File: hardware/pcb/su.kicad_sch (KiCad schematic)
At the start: 22 parts, among them Q2 BC817

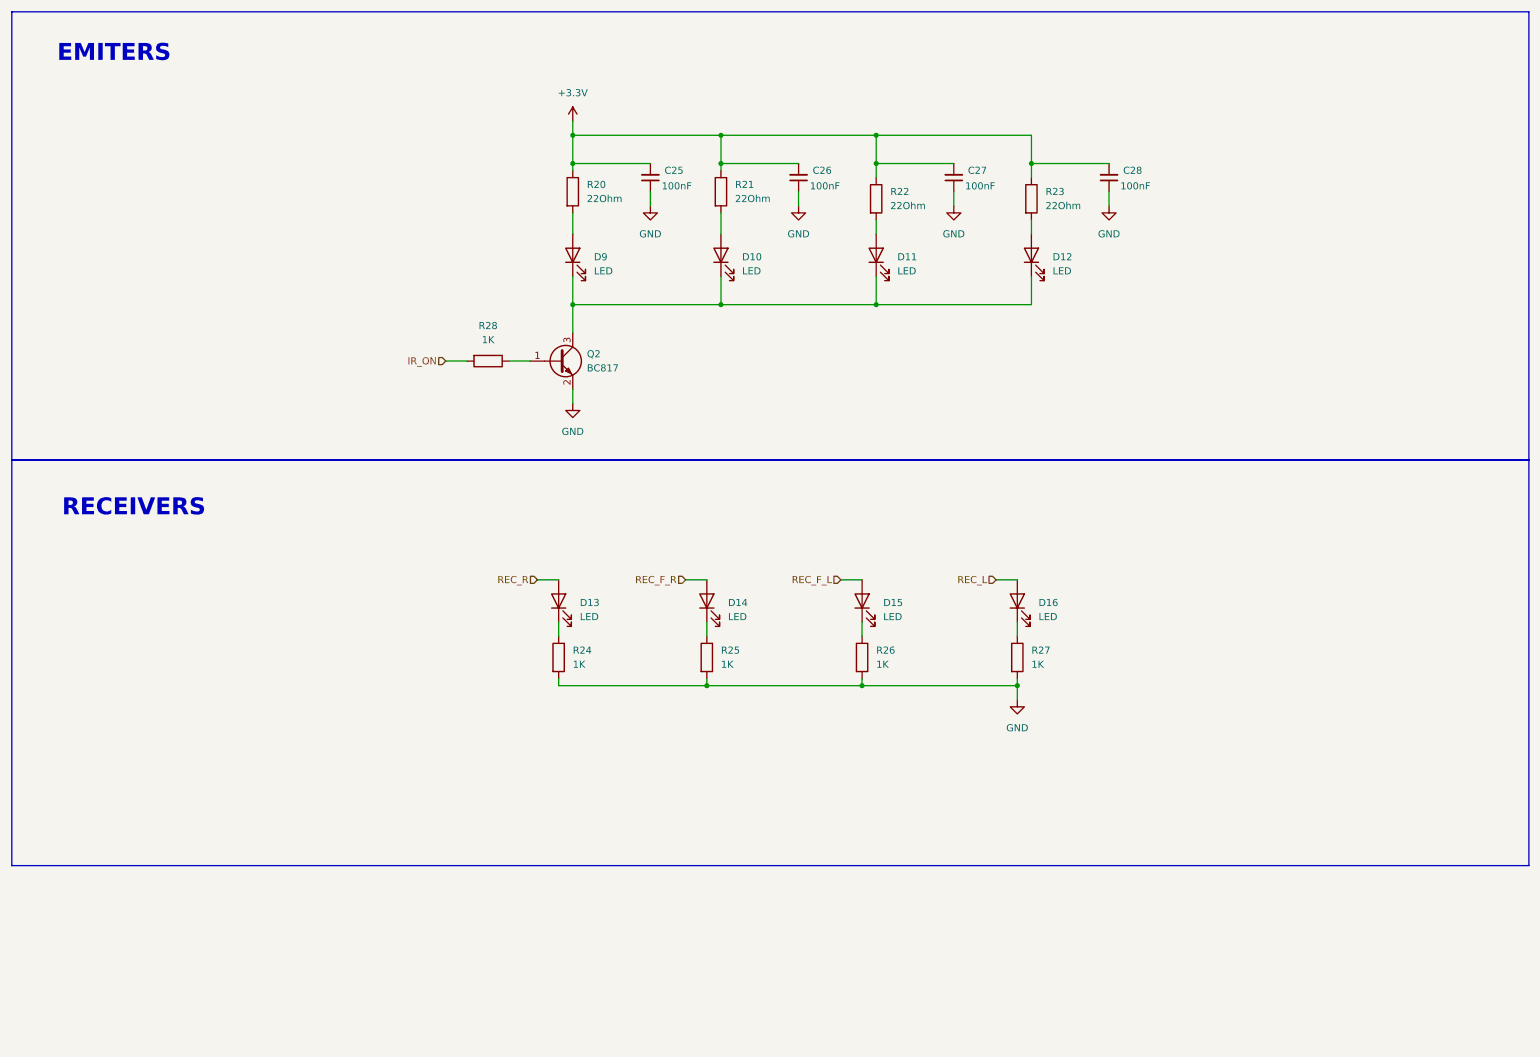
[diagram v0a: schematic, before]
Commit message: hardware: freeze schematic v1 after complete PCB redesign
Complete PCB and schematic refresh with reorganized sheets (psu, ui),
updated MCU/motor/sensor subsystems, and v1 schematic baseline frozen.
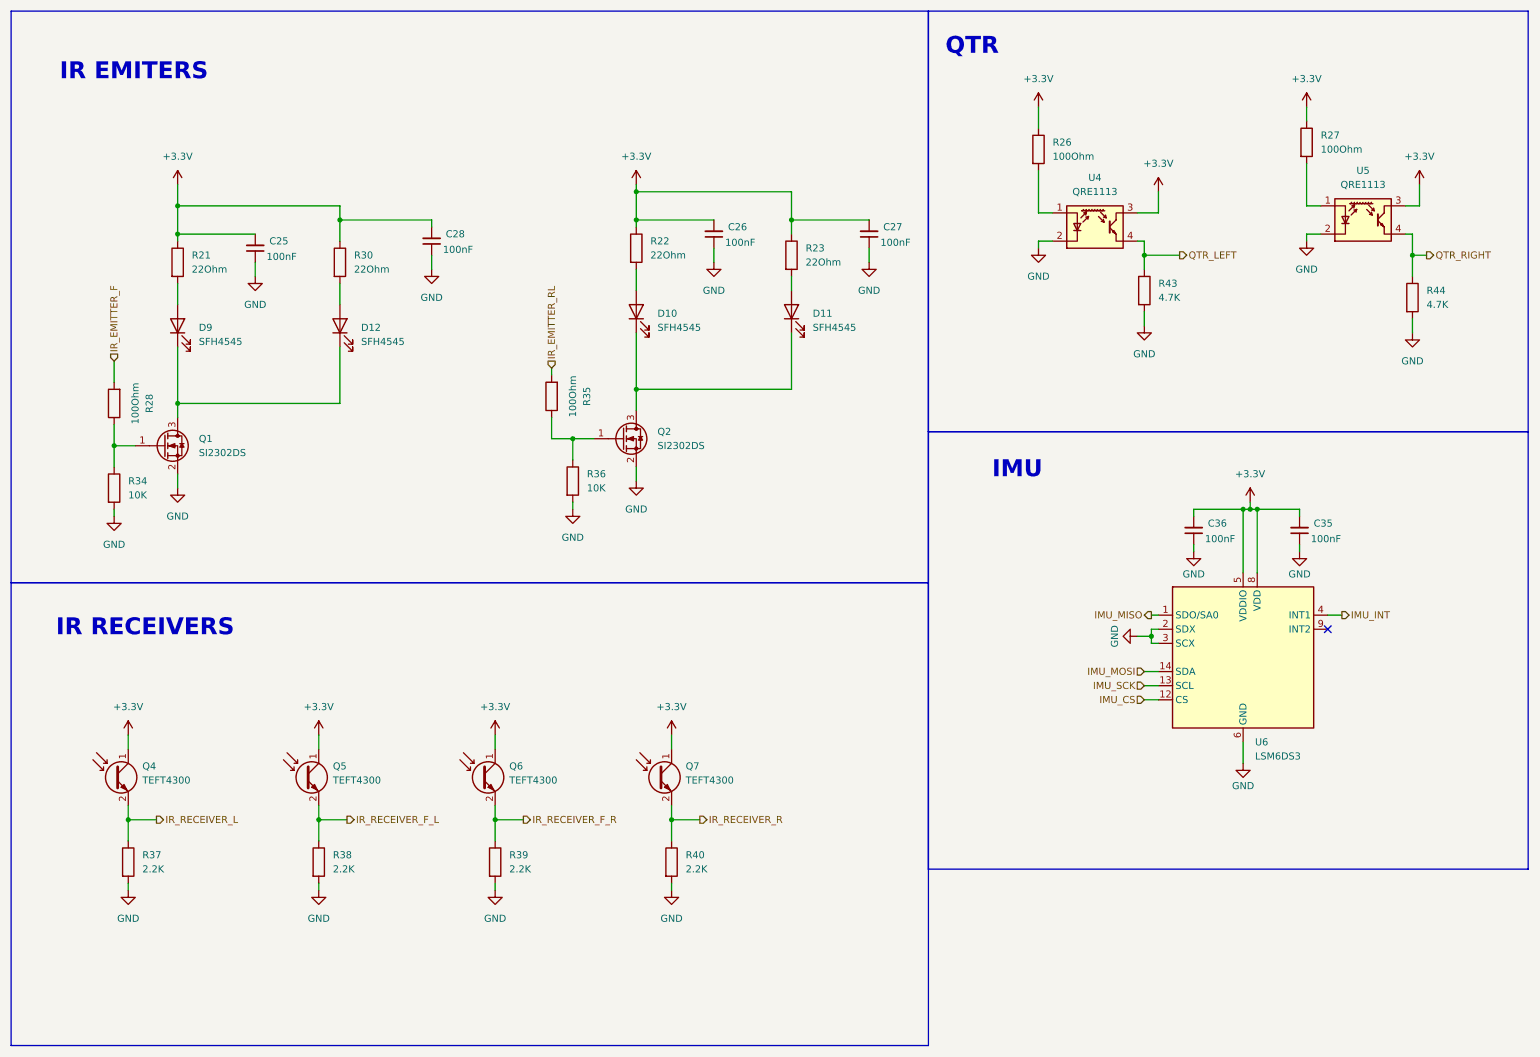
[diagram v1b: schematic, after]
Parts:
- removed D13, D14, D15, D16: LED, LED_THT:LED_D5.0mm, symbol Device:LED
- removed Q2: BC817, Package_TO_SOT_SMD:SOT-23, symbol Transistor_BJT:BC817
- removed R20: 22Ohm, Resistor_SMD:R_0805_2012Metric_Pad1.20x1.40mm_HandSolder, symbol Device:R
- removed R24, R25: 1K, Resistor_SMD:R_0805_2012Metric_Pad1.20x1.40mm_HandSolder, symbol Device:R
- added C35, C36: 100nF, Capacitor_SMD:C_0805_2012Metric_Pad1.18x1.45mm_HandSolder, symbol Device:C_Small
- added Q1, Q2: SI2302DS, Package_TO_SOT_SMD:SOT-23, symbol Transistor_FET:Q_NMOS_GSD
- added Q4, Q5, Q6, Q7: TEFT4300, LED_THT:LED_D3.0mm_IRBlack, symbol Device:Q_Photo_NPN
- added R30: 22Ohm, Resistor_SMD:R_1206_3216Metric_Pad1.30x1.75mm_HandSolder, symbol Device:R
- added R34, R36: 10K, Resistor_SMD:R_0805_2012Metric_Pad1.20x1.40mm_HandSolder, symbol Device:R
- added R35: 100Ohm, Resistor_SMD:R_0805_2012Metric_Pad1.20x1.40mm_HandSolder, symbol Device:R
- added R37, R38, R39, R40: 2.2K, Resistor_SMD:R_0805_2012Metric_Pad1.20x1.40mm_HandSolder, symbol Device:R
- added R43, R44: 4.7K, Resistor_SMD:R_0805_2012Metric_Pad1.20x1.40mm_HandSolder, symbol Device:R
- added U4, U5: QRE1113, OptoDevice:OnSemi_CASE100AQ, symbol Sensor_Proximity:QRE1113
- added U6: LSM6DS3, Package_LGA:LGA-14_3x2.5mm_P0.5mm_LayoutBorder3x4y, symbol Sensor_Motion:LSM6DS3
- D10, D11, D12, D9: value LED -> SFH4545; footprint LED_THT:LED_D5.0mm -> LED_THT:LED_D5.0mm_Horizontal_O1.27mm_Z15.0mm
- R21, R22, R23: footprint Resistor_SMD:R_0805_2012Metric_Pad1.20x1.40mm_HandSolder -> Resistor_SMD:R_1206_3216Metric_Pad1.30x1.75mm_HandSolder
- R26, R27: value 1K -> 100Ohm; footprint Resistor_SMD:R_0805_2012Metric_Pad1.20x1.40mm_HandSolder -> Resistor_SMD:R_1206_3216Metric_Pad1.30x1.75mm_HandSolder
- R28: value 1K -> 100Ohm
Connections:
- net +3.3V: now also R26.1, R27.1, C35.2, C36.2, Q4.1 (C), Q5.1 (C), Q6.1 (C), Q7.1 (C), R30.1, U4.3, U5.3, U6.5 (VDDIO), U6.8 (VDD)
- net GND: now also C35.1, C36.1, Q1.2 (S), Q2.2 (S), R34.2, R36.2, R37.2, R38.2, R39.2, R40.2, R43.2, R44.2, U4.2 (K), U5.2 (K), U6.2 (SDX), U6.3 (SCX), U6.6 (GND), U6.7 (GND); no longer R26.2, R27.2
- net at D10.1 (K), D11.1 (K): now also Q2.3 (D); no longer D12.1 (K), D9.1 (K)
- net at D12.2 (A): now also R30.2; no longer R23.2
- net at R28.1: now also Q1.1 (G), R34.1
- net at R22.2: now also D10.2 (A); no longer D11.2 (A)
- net at D9.2 (A): now also R21.2
- net IR_ON renamed IR_EMITTER_F
- new net: R27.2, U5.1 (A)
- new net: Q2.1 (G), R35.1, R36.1
- new net: R26.2, U4.1 (A)
- new net: D12.1 (K), D9.1 (K), Q1.3 (D)
- new net: D11.2 (A), R23.2
- new net IMU_CS: U6.12 (CS)
- new net IMU_INT: U6.4 (INT1)
- new net IMU_MISO: U6.1 (SDO/SA0)
- new net IMU_MOSI: U6.14 (SDA)
- new net IMU_SCK: U6.13 (SCL)
- new net IR_EMITTER_RL: R35.2
- new net IR_RECEIVER_F_L: Q5.2 (E), R38.1
- new net IR_RECEIVER_F_R: Q6.2 (E), R39.1
- new net IR_RECEIVER_L: Q4.2 (E), R37.1
- new net IR_RECEIVER_R: Q7.2 (E), R40.1
- new net QTR_LEFT: R43.1, U4.4
- new net QTR_RIGHT: R44.1, U5.4
- no-connect marks 0 -> 1
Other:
- note added: "IMU"
- note added: "IR EMITERS"
- note added: "IR RECEIVERS"
- note added: "QTR"
- note removed: "EMITERS"
- note removed: "RECEIVERS"

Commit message: format öncesi commit
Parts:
- C25, C26, C27, C28, C35, C36: footprint Capacitor_SMD:C_0805_2012Metric_Pad1.18x1.45mm_HandSolder -> Capacitor_SMD:C_0603_1608Metric
- R21, R22, R23, R30: footprint Resistor_SMD:R_1206_3216Metric_Pad1.30x1.75mm_HandSolder -> Resistor_SMD:R_1206_3216Metric
- R26, R27: footprint Resistor_SMD:R_1206_3216Metric_Pad1.30x1.75mm_HandSolder -> Resistor_SMD:R_0603_1608Metric
- R28, R34, R35, R36, R37, R38, R39, R40, R43, R44: footprint Resistor_SMD:R_0805_2012Metric_Pad1.20x1.40mm_HandSolder -> Resistor_SMD:R_0603_1608Metric
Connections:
- net at D11.1 (K), Q2.3 (D): now also D12.1 (K); no longer D10.1 (K)
- net at R22.2: now also D11.2 (A); no longer D10.2 (A)
- net at R30.2: now also D10.2 (A); no longer D12.2 (A)
- net at D9.1 (K), Q1.3 (D): now also D10.1 (K); no longer D12.1 (K)
- net at R23.2: now also D12.2 (A); no longer D11.2 (A)
